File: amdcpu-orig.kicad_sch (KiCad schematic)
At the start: 0 parts

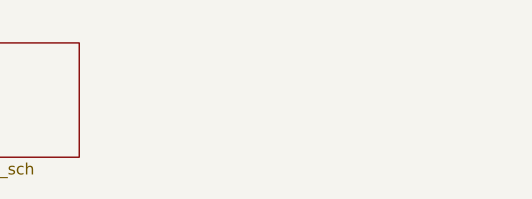
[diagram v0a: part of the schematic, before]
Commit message: Start with ALU sheet
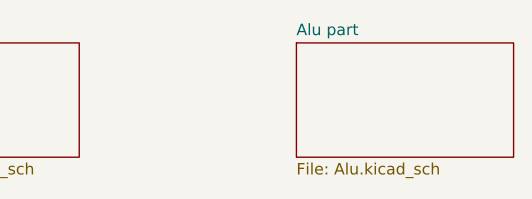
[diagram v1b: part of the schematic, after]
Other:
- added sheet Alu part (Alu.kicad_sch)
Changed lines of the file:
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@@
+	)
+	(sheet
+		(at 80.01 29.21)
+		(size 24.13 12.7)
+		(exclude_from_sim no)
+		(in_bom yes)
+		(on_board yes)
+		(dnp no)
+		(fields_autoplaced yes)
+		(stroke
+			(width 0.1524)
+			(type solid)
+		)
+		(fill
+			(color 0 0 0 0)
+		)
+		(property "Sheetname" "Alu part"
+			(at 80.01 28.4984 0)
+			(show_name no)
+			(do_not_autoplace no)
+			(effects
+				(font
+					(size 1.27 1.27)
+				)
+				(justify left bottom)
+			)
+		)
+		(property "Sheetfile" "Alu.kicad_sch"
+			(at 80.01 42.4946 0)
+			(show_name no)
+			(do_not_autoplace no)
+			(effects
+				(font
+					(size 1.27 1.27)
+				)
+				(justify left top)
+			)
+		)
+		(instances
+			(project "amdcpu-orig"
+				(path "/3b020b28-2b1a-4640-a139-d2fa6eea1e27"
+					(page "3")
+				)
+			)
+		)
 	)
 	(sheet

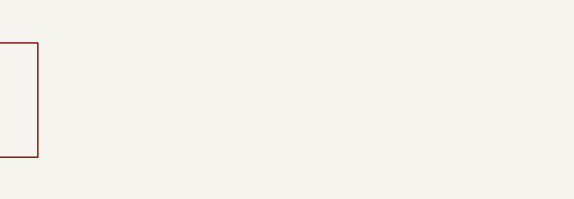
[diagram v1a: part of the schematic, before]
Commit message: More parts of the schema
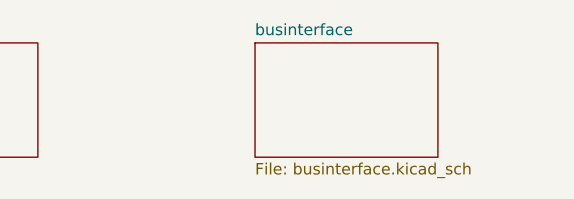
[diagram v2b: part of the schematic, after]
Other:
- added sheet businterface (businterface.kicad_sch)
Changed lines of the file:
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@@
+	)
+	(sheet
+		(at 128.27 29.21)
+		(size 20.32 12.7)
+		(exclude_from_sim no)
+		(in_bom yes)
+		(on_board yes)
+		(dnp no)
+		(fields_autoplaced yes)
+		(stroke
+			(width 0.1524)
+			(type solid)
+		)
+		(fill
+			(color 0 0 0 0)
+		)
+		(property "Sheetname" "businterface"
+			(at 128.27 28.4984 0)
+			(show_name no)
+			(do_not_autoplace no)
+			(effects
+				(font
+					(size 1.27 1.27)
+				)
+				(justify left bottom)
+			)
+		)
+		(property "Sheetfile" "businterface.kicad_sch"
+			(at 128.27 42.4946 0)
+			(show_name no)
+			(do_not_autoplace no)
+			(effects
+				(font
+					(size 1.27 1.27)
+				)
+				(justify left top)
+			)
+		)
+		(instances
+			(project "amdcpu-orig"
+				(path "/3b020b28-2b1a-4640-a139-d2fa6eea1e27"
+					(page "4")
+				)
+			)
+		)
 	)
 	(sheet

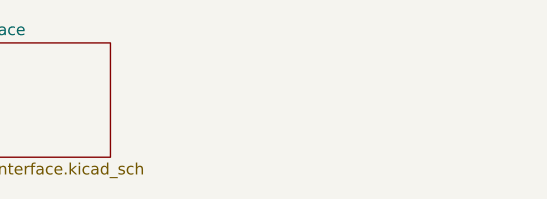
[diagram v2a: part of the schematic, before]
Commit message: Schematic complete wrt original
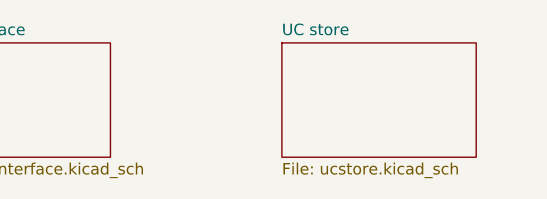
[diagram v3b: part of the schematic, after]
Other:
- added sheet UC store (ucstore.kicad_sch)
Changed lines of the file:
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@@
+	)
+	(sheet
+		(at 167.64 29.21)
+		(size 21.59 12.7)
+		(exclude_from_sim no)
+		(in_bom yes)
+		(on_board yes)
+		(dnp no)
+		(fields_autoplaced yes)
+		(stroke
+			(width 0.1524)
+			(type solid)
+		)
+		(fill
+			(color 0 0 0 0)
+		)
+		(property "Sheetname" "UC store"
+			(at 167.64 28.4984 0)
+			(show_name no)
+			(do_not_autoplace no)
+			(effects
+				(font
+					(size 1.27 1.27)
+				)
+				(justify left bottom)
+			)
+		)
+		(property "Sheetfile" "ucstore.kicad_sch"
+			(at 167.64 42.4946 0)
+			(show_name no)
+			(do_not_autoplace no)
+			(effects
+				(font
+					(size 1.27 1.27)
+				)
+				(justify left top)
+			)
+		)
+		(instances
+			(project "amdcpu-orig"
+				(path "/3b020b28-2b1a-4640-a139-d2fa6eea1e27"
+					(page "5")
+				)
+			)
+		)
 	)
 	(sheet

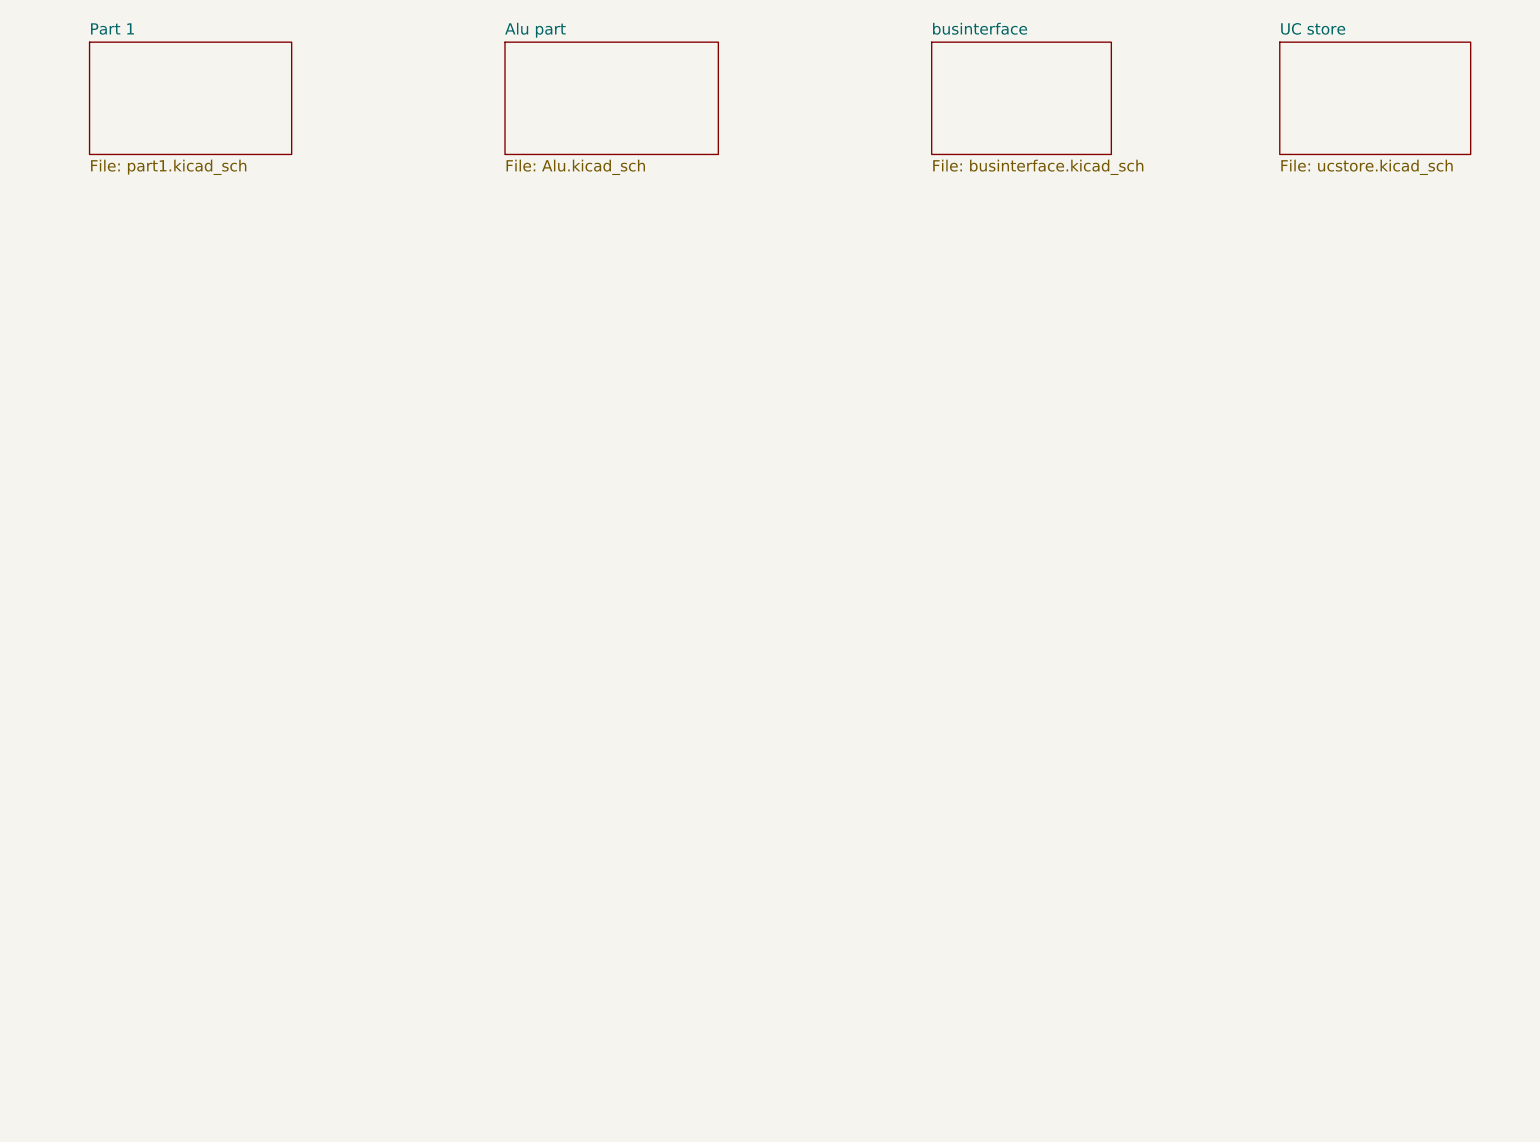
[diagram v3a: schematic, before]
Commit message: Annotate a lot of the schematic with functional descs
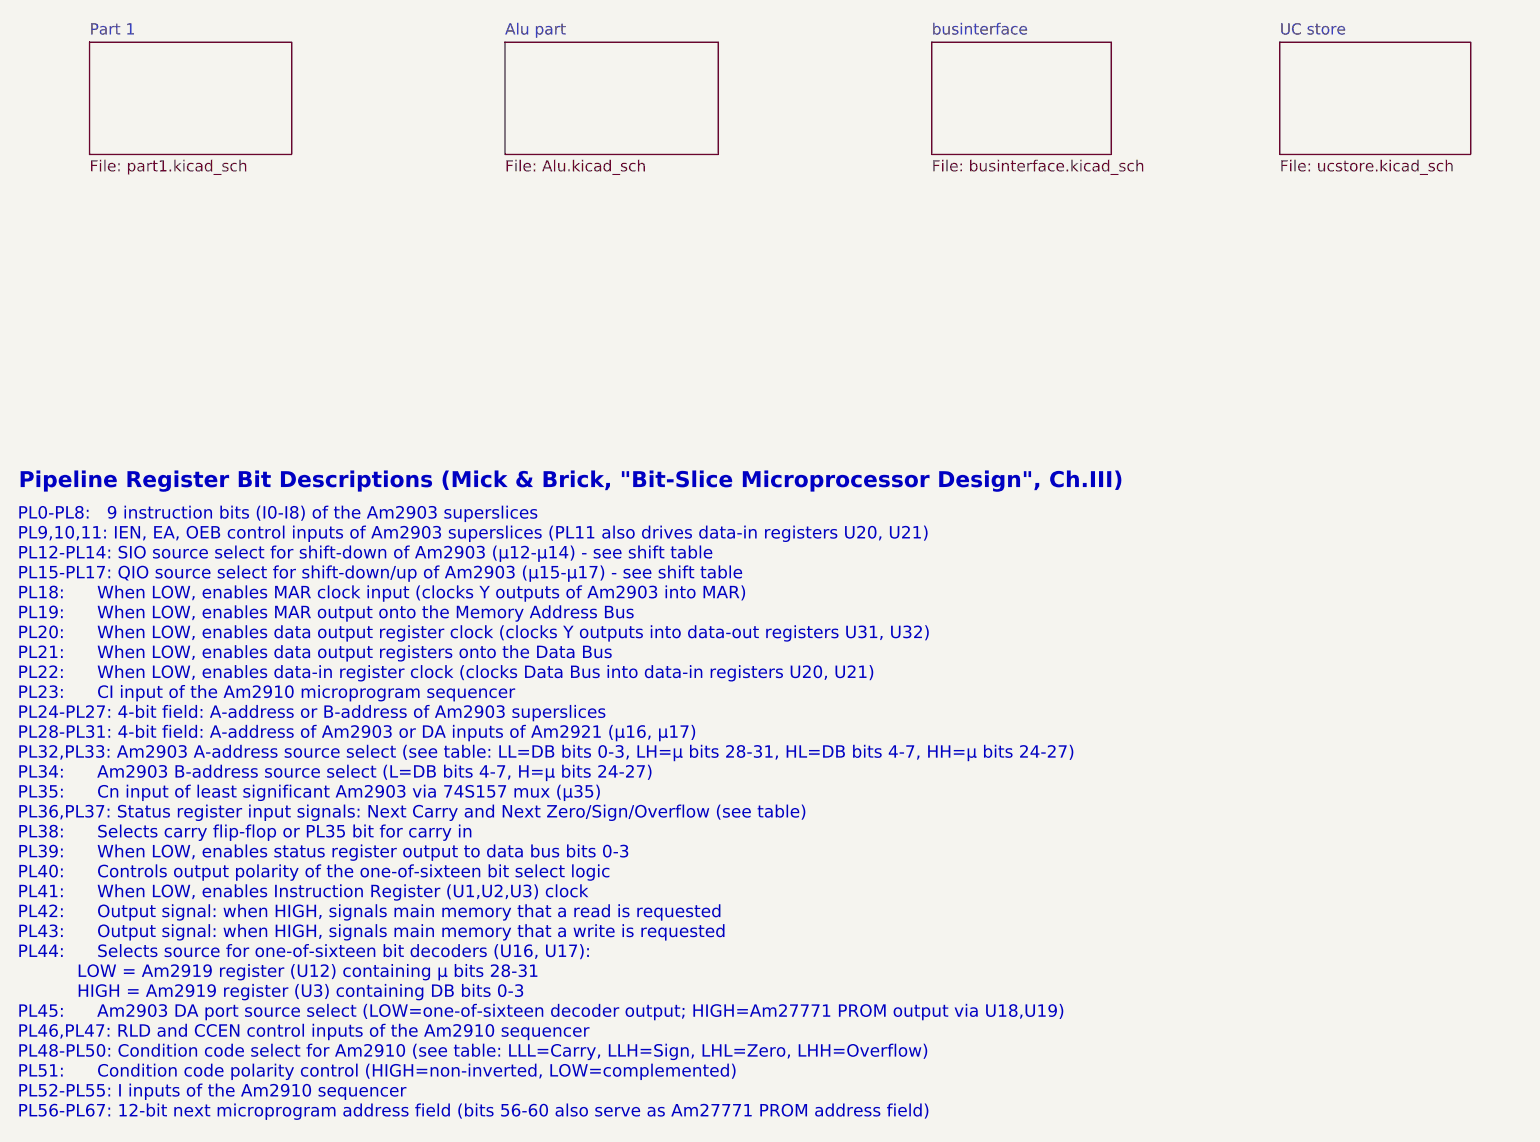
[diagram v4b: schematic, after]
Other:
- note added: "PL0-PL8: 9 instruction bits (I0-I8) of the Am2903 superslices PL9,10,11: IEN, EA, OEB control inputs of Am2903 superslices (PL11 also drives data-in registers U20, U21) PL12-PL14: SIO source select for shift-down of Am2903 (µ12-µ14) - see shift table PL15-PL17: QIO source select for shift-down/up of Am2903 (µ15-µ17) - see shift table PL18: When LOW, enables MAR clock input (clocks Y outputs of Am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"
- note added: "Pipeline Register Bit Descriptions (Mick & Brick, "Bit-Slice Microprocessor Design", Ch.III)"
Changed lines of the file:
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@@
 		(rev "0.1")
+	)
+	(text "Pipeline Register Bit Descriptions (Mick & Brick, \"Bit-Slice Microprocessor Design\", Ch.III)"
+		(exclude_from_sim no)
+		(at 25 80 0)
+		(effects
+			(font
+				(size 1.8 1.8)
+				(bold yes)
+			)
+			(justify left bottom)
+		)
+	)
+	(text "PL0-PL8:   9 instruction bits (I0-I8) of the Am2903 superslices\nPL9,10,11: IEN, EA, OEB control inputs of Am2903 superslices (PL11 also drives data-in registers U20, U21)\nPL12-PL14: SIO source select for shift-down of Am2903 (µ12-µ14) - see shift table\nPL15-PL17: QIO source select for shift-down/up of Am2903 (µ15-µ17) - see shift table\nPL18:      When LOW, enables MAR clock input (clocks Y outputs of Am2903 into MAR)\nPL19:      When LOW, enables MAR output onto the Memory Address Bus\nPL20:      When LOW, enables data output register clock (clocks Y outputs into data-out registers U31, U32)\nPL21:      When LOW, enables data output registers onto the Data Bus\nPL22:      When LOW, enables data-in register clock (clocks Data Bus into data-in registers U20, U21)\nPL23:      CI input of the Am2910 microprogram sequencer\nPL24-PL27: 4-bit field: A-address or B-address of Am2903 superslices\nPL28-PL31: 4-bit field: A-address of Am2903 or DA inputs of Am2921 (µ16, µ17)\nPL32,PL33: Am2903 A-address source select (see table: LL=DB bits 0-3, LH=µ bits 28-31, HL=DB bits 4-7, HH=µ bits 24-27)\nPL34:      Am2903 B-address source select (L=DB bits 4-7, H=µ bits 24-27)\nPL35:      Cn input of least significant Am2903 via 74S157 mux (µ35)\nPL36,PL37: Status register input signals: Next Carry and Next Zero/Sign/Overflow (see table)\nPL38:      Selects carry flip-flop or PL35 bit for carry in\nPL39:      When LOW, enables status register output to data bus bits 0-3\nPL40:      Controls output polarity of the one-of-sixteen bit select logic\nPL41:      When LOW, enables Instruction Register (U1,U2,U3) clock\nPL42:      Output signal: when HIGH, signals main memory that a read is requested\nPL43:      Output signal: when HIGH, signals main memory that a write is requested\nPL44:      Selects source for one-of-sixteen bit decoders (U16, U17):\n           LOW = Am2919 register (U12) containing µ bits 28-31\n           HIGH = Am2919 register (U3) containing DB bits 0-3\nPL45:      Am2903 DA port source select (LOW=one-of-sixteen decoder output; HIGH=Am27771 PROM output via U18,U19)\nPL46,PL47: RLD and CCEN control inputs of the Am2910 sequencer\nPL48-PL50: Condition code select for Am2910 (see table: LLL=Carry, LLH=Sign, LHL=Zero, LHH=Overflow)\nPL51:      Condition code polarity control (HIGH=non-inverted, LOW=complemented)\nPL52-PL55: I inputs of the Am2910 sequencer\nPL56-PL67: 12-bit next microprogram address field (bits 56-60 also serve as Am27771 PROM address field)"
+		(exclude_from_sim no)
+		(at 24.892 151.13 0)
+		(effects
+			(font
+				(size 1.4 1.4)
+			)
+			(justify left bottom)
+		)
 	)
 	(sheet
